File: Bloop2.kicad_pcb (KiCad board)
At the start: 2 copper layers, 49.5 x 43.8 mm, 32 parts, among them J1 Power In, J2 Input, J3 Return, J4 Send, J5 Output, SW1 3PDTA, SW2 3PDTB, SW3 3PDTC, U1 TL072

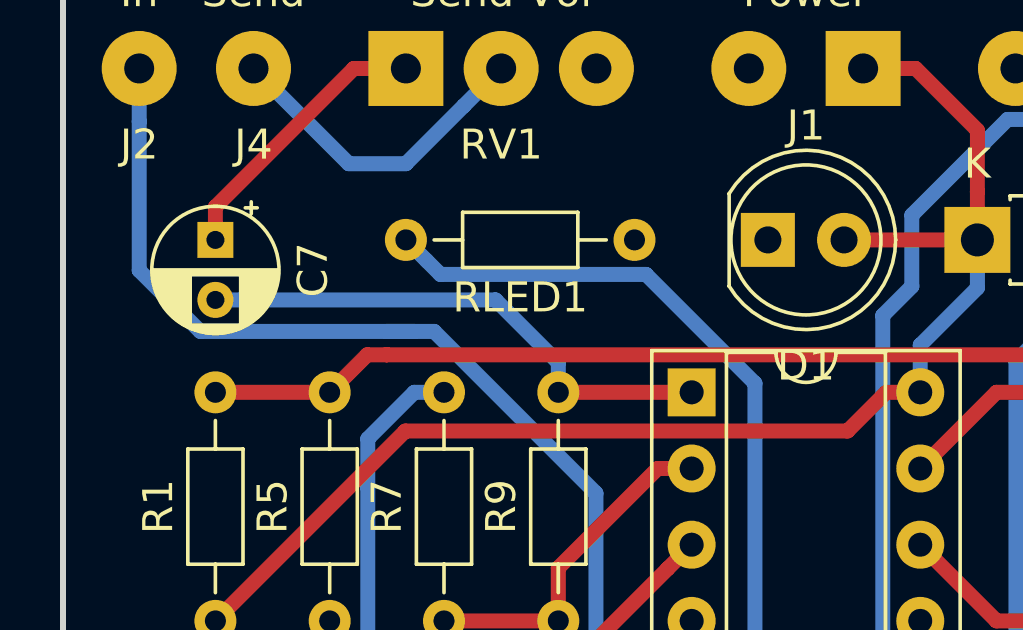
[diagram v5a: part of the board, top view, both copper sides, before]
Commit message: Fix a few PCB labels
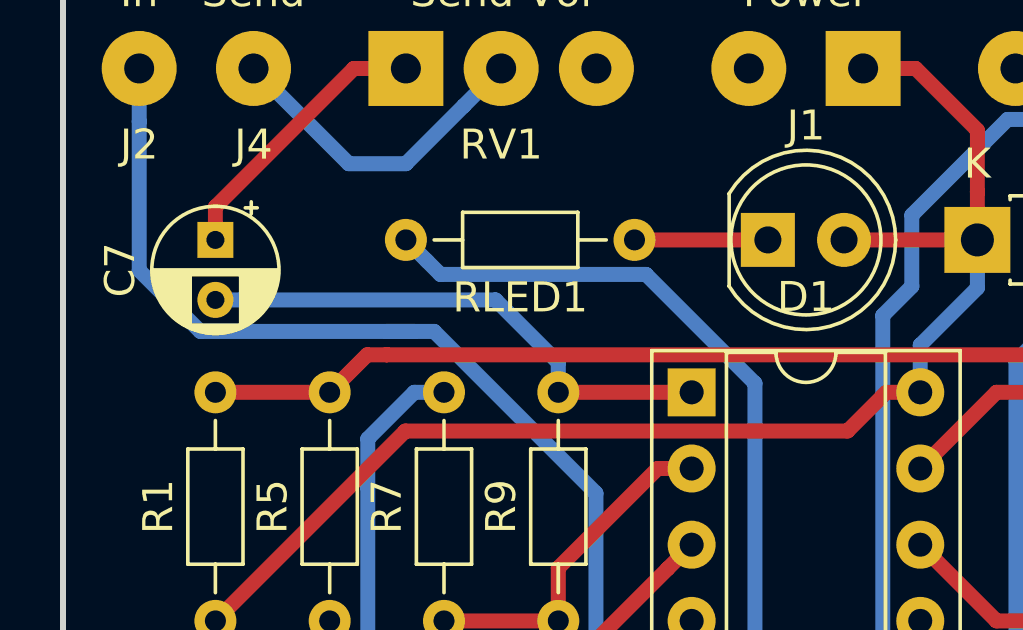
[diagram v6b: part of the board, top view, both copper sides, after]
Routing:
- net Net-(D1-Pad1): track 0.00 -> 4.44 mm
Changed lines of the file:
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@@
     (thickness 1.6)
     (drawings 47)
-    (tracks 113)
+    (tracks 114)
     (zones 0)
     (modules 32)
@@
     (descr "LED, diameter 5.0mm, 2 pins, http://cdn-reichelt.de/documents/datenblatt/A500/LL-504BC2E-009.pdf")
     (tags "LED diameter 5.0mm 2 pins")
-    (fp_text reference D1 (at 1.27 4.191) (layer F.SilkS)
+    (fp_text reference D1 (at 1.27 1.905) (layer F.SilkS)
       (effects (font (size 1 1) (thickness 0.15)))
     )
@@
     (descr "CP, Radial series, Radial, pin pitch=2.00mm, , diameter=4mm, Electrolytic Capacitor")
     (tags "CP Radial series Radial pin pitch 2.00mm  diameter 4mm Electrolytic Capacitor")
-    (fp_text reference C7 (at 1 -3.25 270) (layer F.SilkS)
+    (fp_text reference C7 (at 1 3.175 270) (layer F.SilkS)
       (effects (font (size 1 1) (thickness 0.15)))
     )
@@
   (segment (start 173.355 100.33) (end 170.815 97.79) (width 0.5) (layer B.Cu) (net 9))
   (segment (start 173.355 121.285) (end 173.355 100.33) (width 0.5) (layer B.Cu) (net 9))
+  (segment (start 153.035 92.71) (end 157.48 92.71) (width 0.5) (layer F.Cu) (net 10))
   (segment (start 165.299999 116.225001) (end 164.05 117.475) (width 0.5) (layer B.Cu) (net 11))
   (segment (start 165.750001 115.774999) (end 165.299999 116.225001) (width 0.5) (layer B.Cu) (net 11))

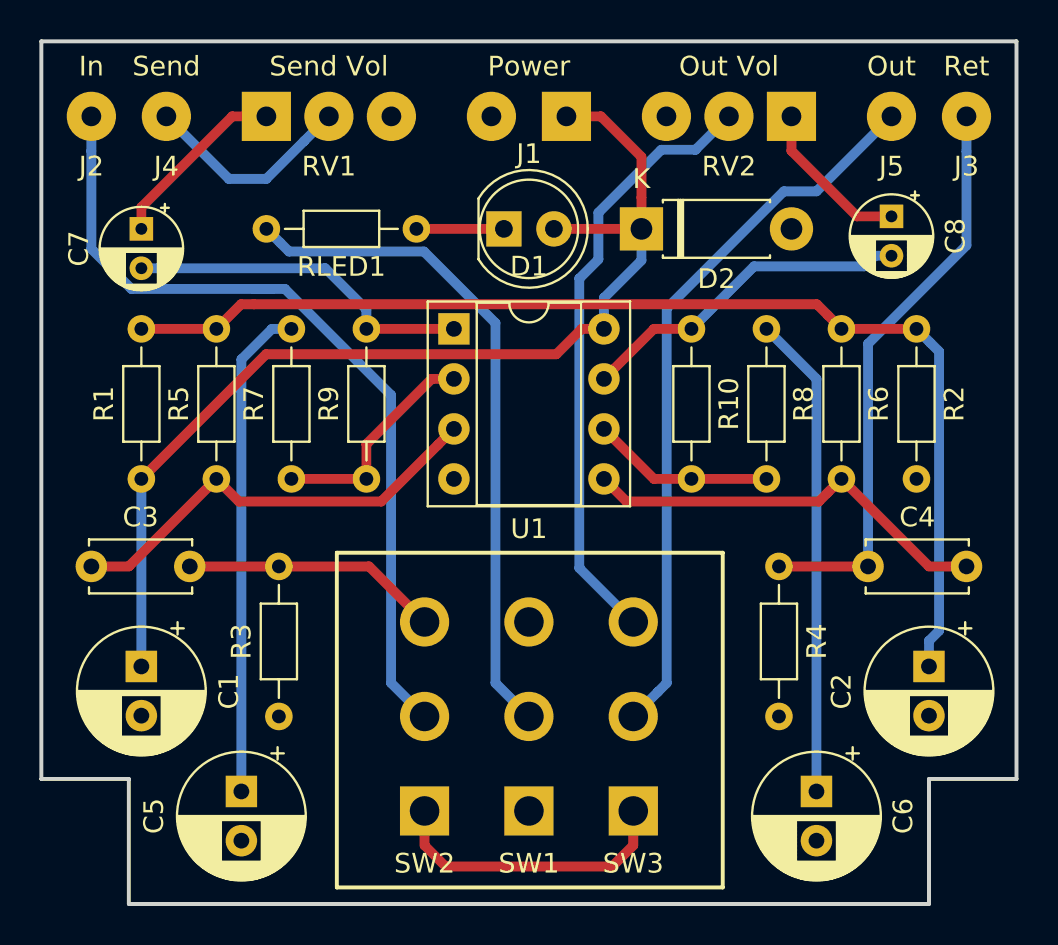
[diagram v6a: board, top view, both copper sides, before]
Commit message: Specify polar output caps.
Output cap type seems to have a significant effect on EQ. I'd like to leave this as an option for the builder, but leaving the schematic symbols non-polarized results in a backwards footprint on the PCB.
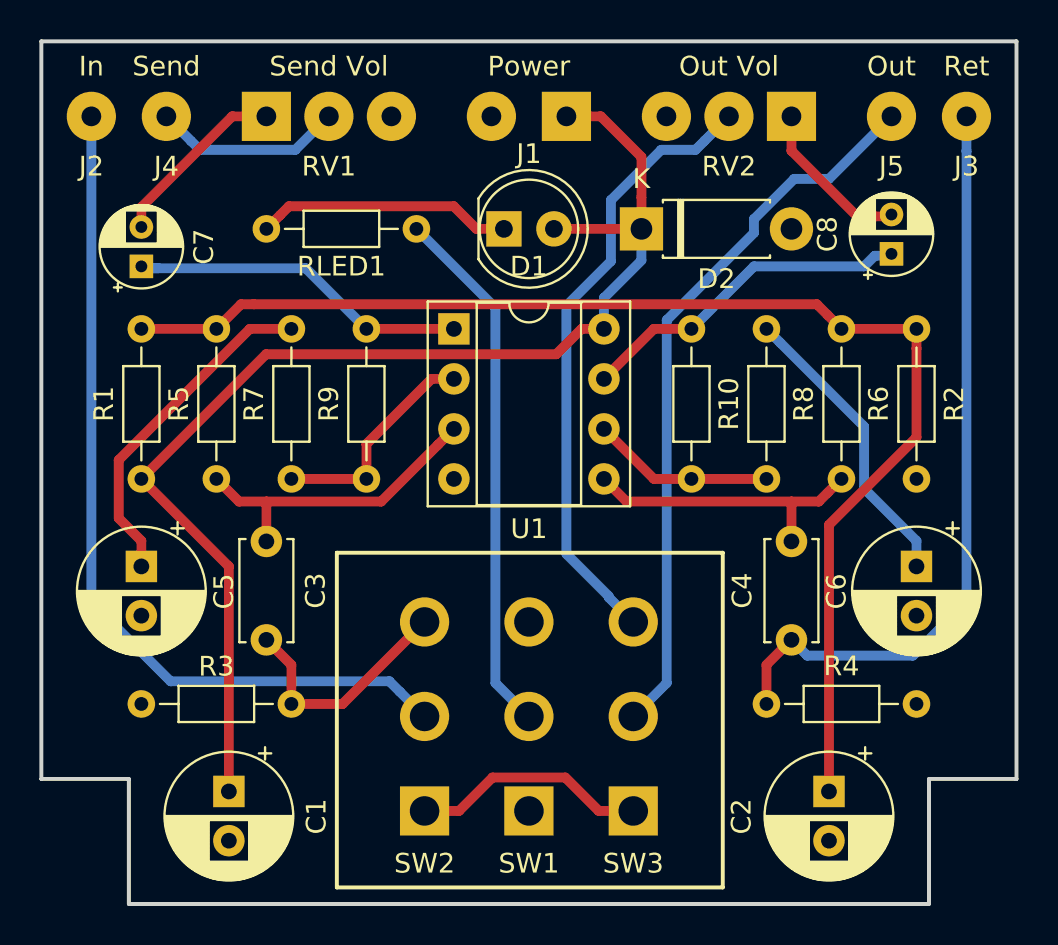
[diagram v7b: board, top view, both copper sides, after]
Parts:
- moved C5 12.5 mm to (139.1, 109.9)
- moved C6 12.5 mm to (178.4, 109.9)
- moved C3 8.98 mm to (145.4, 108.6), turned to 270 degrees
- moved C4 8.98 mm to (172.1, 108.6), turned to 270 degrees
- moved C2 8.13 mm to (174.0, 121.3)
- moved C1 7.75 mm to (143.5, 121.3)
- moved RLED1 7.62 mm to (145.4, 92.7), turned to 0 degrees
- moved R3 7.01 mm to (146.7, 116.8), turned to 180 degrees
- moved R4 7.01 mm to (170.8, 116.8), turned to 0 degrees
- moved C7 1.91 mm to (139.1, 94.6), turned to 90 degrees
- moved C8 1.91 mm to (177.2, 94.0), turned to 90 degrees
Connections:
- R10 pad 2: Net-(C8-Pad2) -> Net-(C8-Pad1)
- R9 pad 2: Net-(C7-Pad2) -> Net-(C7-Pad1)
- RV1 pad 1: Net-(C7-Pad1) -> Net-(C7-Pad2)
- RV2 pad 1: Net-(C8-Pad1) -> Net-(C8-Pad2)
- U1 pad 1: Net-(C7-Pad2) -> Net-(C7-Pad1)
- U1 pad 7: Net-(C8-Pad2) -> Net-(C8-Pad1)
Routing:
- net Net-(C4-Pad2): track 29.5 -> 38.8 mm
- net Net-(C6-Pad1): track 24.5 -> 15.2 mm
- net Net-(C8-Pad2): track 17.2 -> 8.21 mm
- net Net-(C8-Pad1): track 8.21 -> 17.2 mm
- net Net-(C7-Pad1): track 9.36 -> 18.0 mm
- net Net-(D1-Pad1): track 4.44 -> 13.0 mm
- net Net-(C7-Pad2): track 17.7 -> 9.36 mm
- net +9V: track 54.8 -> 63.0 mm
- net Net-(C5-Pad1): track 25.1 -> 17.4 mm
- net VREF: track 58.3 -> 65.8 mm
- net Net-(RLED1-Pad2): track 34.3 -> 27.1 mm
- net Net-(C4-Pad1): track 21.2 -> 15.0 mm
- net Net-(C3-Pad1): track 22.3 -> 16.1 mm
- net BYPASS: track 15.0 -> 12.0 mm
- net Net-(J4-Pad1): track 10.9 -> 9.66 mm
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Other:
- board text added: "Boosted Loop Switcher"
- board text added: "©2019 kooima.net"
